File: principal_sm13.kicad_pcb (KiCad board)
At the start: 2 copper layers, 126.6 x 40.7 mm, 99 parts, among them J1 RESOLVER ARM, J2 RESOLVER POLE, J3 MOT ARM, J4 MOT POLE, P12 CONN_10X2, P14 SPI, Q1 BC807, Q2 BC807, Q3 BC807, Q4 BC807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

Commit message: agregado logo OSHW y nomy nombre poncho
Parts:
- added REF**: OSHW-Logo2_9.8x8mm_SilkScreen, Symbol:OSHW-Logo2_9.8x8mm_SilkScreen, F.Cu at (165.1, 106.2)
- moved LOGO 3.50 mm to (161.7, 131.4)
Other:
- board text added: "18/07/2020"
- board text added: "PONCHO"
- board text added: "RDC Rev 1.0"

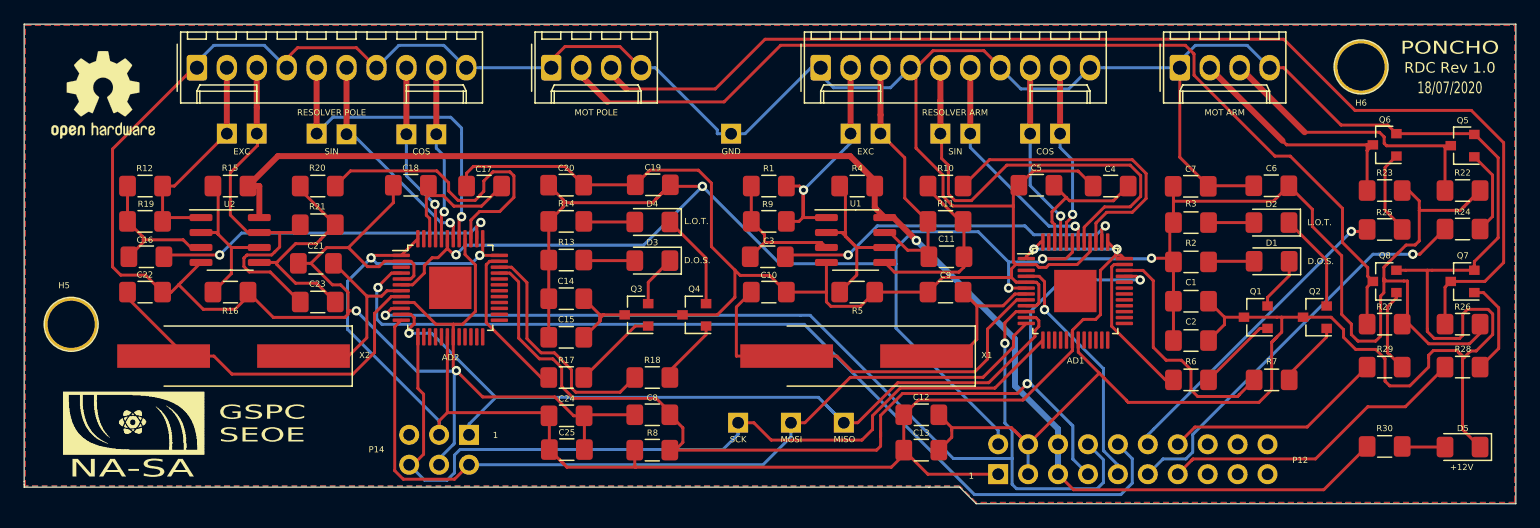
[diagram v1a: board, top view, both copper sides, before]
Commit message: movido texto poncho y alejada pista alrededor de H6
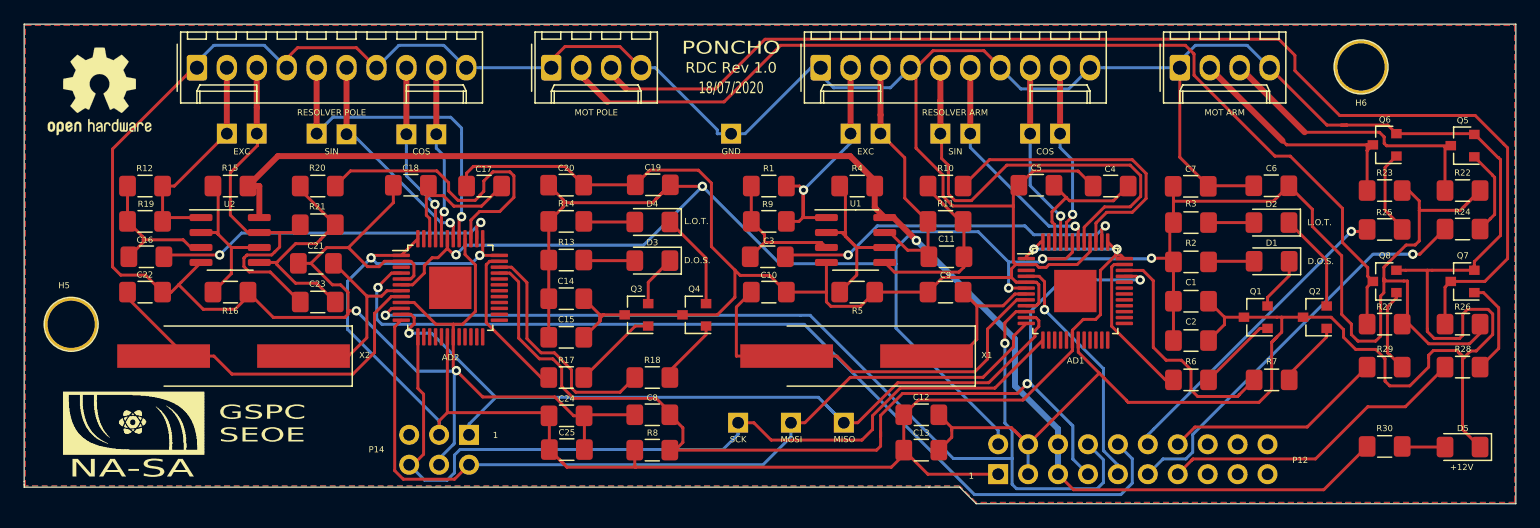
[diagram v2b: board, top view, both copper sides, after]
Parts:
- moved REF** 0.42 mm to (164.8, 105.9)
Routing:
- net Net-(J4-Pad3): track 101.3 -> 102.3 mm
- net GND: track 530.8 -> 531.5 mm

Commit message: modificado cambiador de nivel de salida, agregados TP para los gpio STEP y DIRECTION de los motore PAP
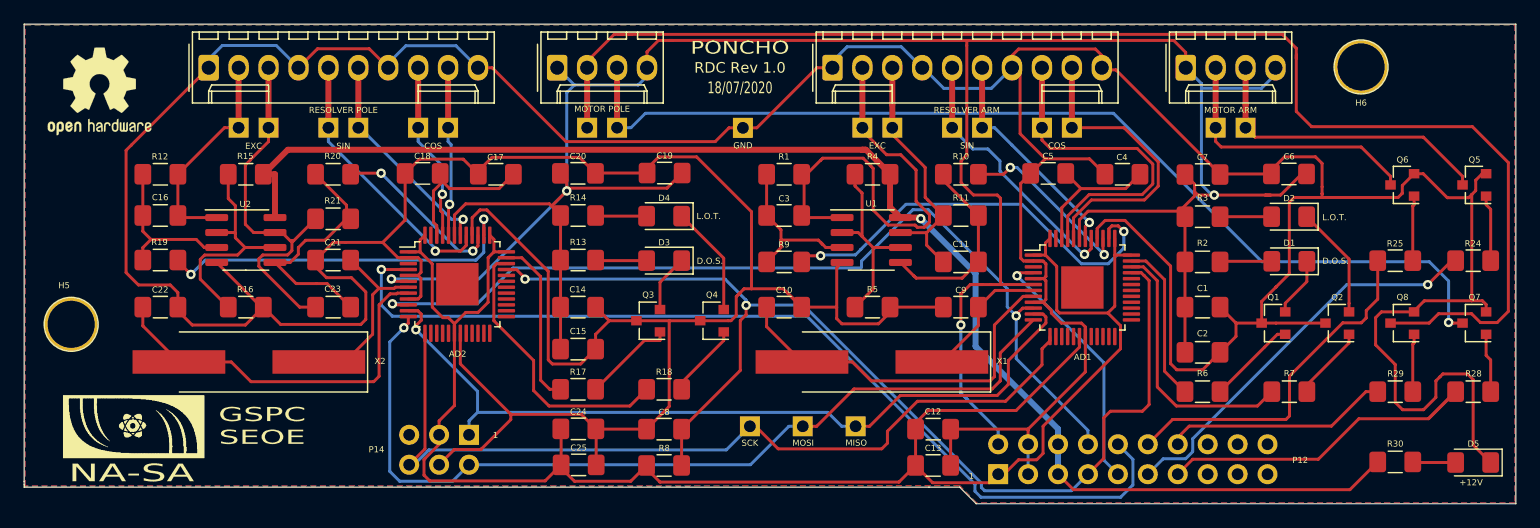
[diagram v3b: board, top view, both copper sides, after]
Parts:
- removed R22, R23, R26, R27: 1K, Resistor_SMD:R_1206_3216Metric_Pad1.42x1.75mm_HandSolder
- added TP17: TPGPIO5, TestPoint:TestPoint_reducido, F.Cu at (259.5, 109.0)
- added TP18: TPGPIO4, TestPoint:TestPoint_reducido, F.Cu at (262.0, 109.0)
- added TP19: TPGPIO7, TestPoint:TestPoint_reducido, F.Cu at (206.2, 109.0)
- added TP20: TPGPIO6, TestPoint:TestPoint_reducido, F.Cu at (208.7, 109.0)
- J3: value MOT ARM -> MOTOR ARM
- J4: value MOT POLE -> MOTOR POLE
- R24, R25, R28, R29: value 10K -> 1K
- moved Q8 3.84 mm to (275.3, 125.5)
- moved Q6 3.72 mm to (275.3, 113.8)
- moved Q7 3.67 mm to (281.5, 125.5)
- moved Q5 3.48 mm to (281.5, 113.8)
- moved R24 2.83 mm to (281.4, 120.2)
- moved R25 2.80 mm to (274.7, 120.2)
- moved R29 2.27 mm to (274.7, 131.4)
- moved R28 2.27 mm to (281.4, 131.4)
- moved Q2 1.96 mm to (269.8, 125.5)
- moved C10 1.82 mm to (222.9, 124.2)
- moved C22 1.82 mm to (169.9, 124.2)
- moved C9 1.82 mm to (237.9, 124.2)
- moved R16 1.82 mm to (177.2, 124.2)
- moved R5 1.82 mm to (230.4, 124.2)
- moved C6 1.80 mm to (265.7, 112.9)
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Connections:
- J3 pad 1: GND -> +5V
- J3 pad 4: GND -> +5V
- J4 pad 1: GND -> +5V
- J4 pad 4: GND -> +5V
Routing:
- net Net-(J4-Pad2): track 86.1 -> 117.4 mm
- net /RDC ARM/SIN: track 40.9 -> 22.9 mm, vias 0 -> 1
- net Net-(C3-Pad1): track 22.4 -> 39.2 mm, vias 1 -> 0
- net +5V: track 209.9 -> 225.6 mm, vias 5 -> 4
- net Net-(J4-Pad3): track 102.3 -> 86.8 mm, vias 0 -> 1
- net /RDC ARM/COS: track 15.9 -> 28.3 mm, vias 1 -> 0
- net GND: track 531.5 -> 519.4 mm, vias 2 -> 0
- net /RDC POLE/~EXC: track 26.7 -> 14.7 mm, vias 0 -> 2
- net +3V3: track 140.5 -> 151.7 mm, vias 4 -> 0
- net /RDC ARM/COSLO: track 15.4 -> 25.7 mm, vias 1 -> 0
- net /GPIO/GPIO1: track 87.9 -> 77.8 mm
- net /RDC ARM/~EXC: track 25.8 -> 16.2 mm, vias 0 -> 2
- net Net-(R15-Pad1): track 14.6 -> 22.3 mm
- net /RDC ARM/EXC: track 30.4 -> 36.6 mm
- net /GPIO/GPIO0: track 90.1 -> 96.1 mm
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
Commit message: alejadas algunas pistas, thermal pads clearance = 0
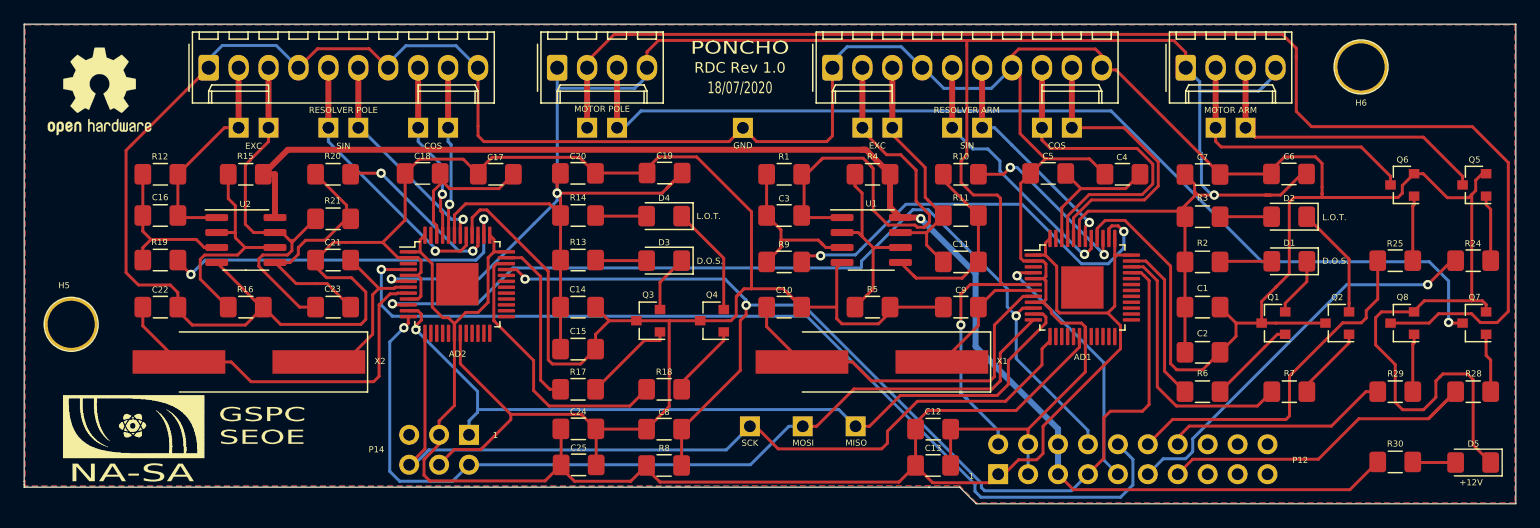
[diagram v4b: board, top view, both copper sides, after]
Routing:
- net GND: track 519.4 -> 527.2 mm
- net +5V: track 225.6 -> 231.7 mm
- net Net-(J4-Pad3): track 86.8 -> 87.6 mm
